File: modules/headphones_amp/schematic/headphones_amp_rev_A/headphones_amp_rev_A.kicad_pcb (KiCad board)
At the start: 2 copper layers, 150 x 100 mm, 113 parts, among them J1 AudioJack3_SwitchTR, J2 AudioJack3_SwitchTR, J3 Conn_01x02, J4 Conn_01x02, J5 Conn_01x02, J6 Conn_01x02, J7 Conn_01x02, Q1 BC140, Q10 BC548, Q11 BC548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

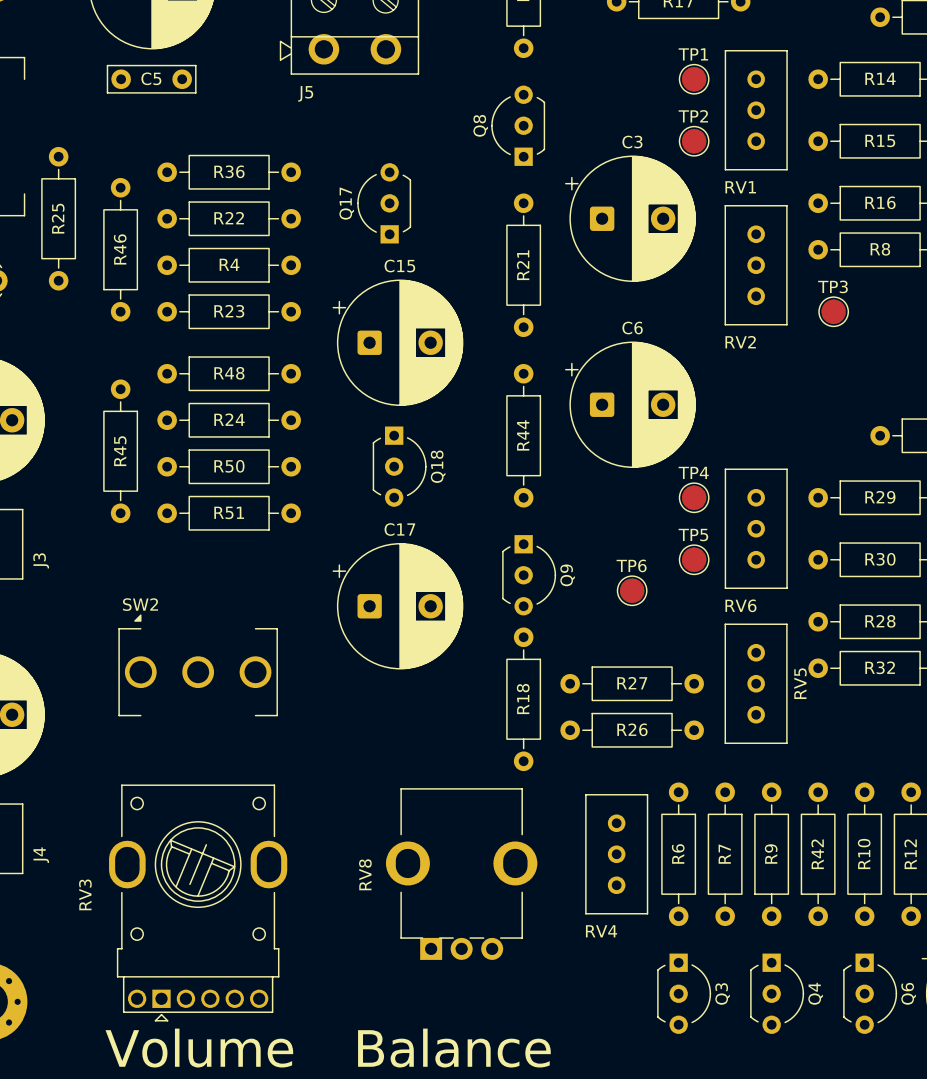
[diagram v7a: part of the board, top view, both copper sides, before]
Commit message: added a PDF export of the schematic
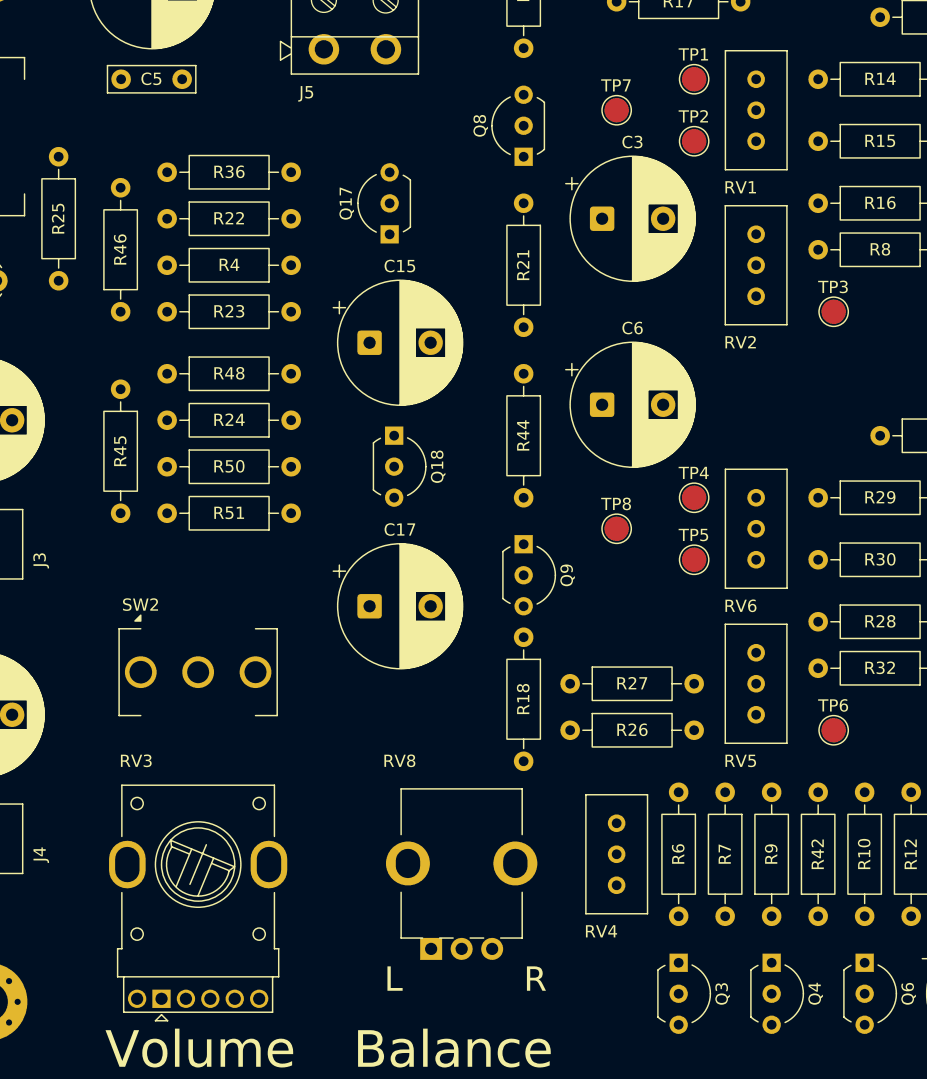
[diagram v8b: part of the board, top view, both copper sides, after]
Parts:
- added TP7: TestPoint, TestPoint:TestPoint_Pad_D2.0mm, F.Cu at (94.0, 44.5)
- added TP8: TestPoint, TestPoint:TestPoint_Pad_D2.0mm, F.Cu at (94.0, 78.7)
- moved TP6 20.1 mm to (111.8, 95.2)
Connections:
- C10 pad 2: Net-(RV3B-W) -> Net-(C10-Pad2)
- C6 pad 1: Net-(C6-Pad1) -> Net-(RV8-B)
- SW2 pad 1: Net-(Q8-C) -> Net-(RV3A-W)
- SW2 pad 2: Net-(C6-Pad1) -> Net-(C10-Pad2)
- SW2 pad 3: Net-(RV8-B) -> Net-(RV3B-W)
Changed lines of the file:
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@@
 	(net 74 "Net-(Q17-C)")
 	(net 75 "Net-(Q18-C)")
-	(net 76 "Net-(C6-Pad1)")
+	(net 76 "Net-(C10-Pad2)")
 	(footprint "Resistor_THT:R_Axial_DIN0207_L6.3mm_D2.5mm_P10.16mm_Horizontal"
 		(layer "F.Cu")
@@
 			(layers "*.Cu" "*.Mask")
 			(remove_unused_layers no)
-			(net 20 "Net-(Q8-C)")
+			(net 65 "Net-(RV3A-W)")
 			(pinfunction "1")
 			(pintype "passive")
@@
 			(layers "*.Cu" "*.Mask")
 			(remove_unused_layers no)
-			(net 76 "Net-(C6-Pad1)")
+			(net 76 "Net-(C10-Pad2)")
 			(pinfunction "2")
 			(pintype "passive")
@@
 			(layers "*.Cu" "*.Mask")
 			(remove_unused_layers no)
-			(net 31 "Net-(RV8-B)")
+			(net 66 "Net-(RV3B-W)")
 			(pinfunction "3")
 			(pintype "passive")
@@
 			(layers "*.Cu" "*.Mask")
 			(remove_unused_layers no)
-			(net 66 "Net-(RV3B-W)")
+			(net 76 "Net-(C10-Pad2)")
 			(pintype "passive")
 		)
@@
 		)
 	)
+	(footprint "TestPoint:TestPoint_Pad_D2.0mm"
+		(layer "F.Cu")
+		(at 93.98 78.74)
+		(descr "SMD pad as test Point, diameter 2.0mm")
+		(tags "test point SMD pad")
+		(property "Reference" "TP8"
+			(at 0 -1.998 0)
+			(layer "F.SilkS")
+			(effects
+				(font
+					(size 1 1)
+					(thickness 0.15)
+				)
+			)
+		)
+		(property "Value" "TestPoint"
+			(at 0 2.05 0)
+			(layer "F.Fab")
+			(hide yes)
+			(effects
+				(font
+					(size 1 1)
+					(thickness 0.15)
+				)
+			)
+		)
+		(property "Datasheet" "~"
+			(at 0 0 0)
+			(unlocked yes)
+			(layer "F.Fab")
+			(hide yes)
+			(effects
+				(font
+					(size 1.27 1.27)
+					(thickness 0.15)
+				)
+			)
+		)
+		(property "Description" "test point"
+			(at 0 0 0)
+			(unlocked yes)
+			(layer "F.Fab")
+			(hide yes)
+			(effects
+				(font
+					(size 1.27 1.27)
+					(thickness 0.15)
+				)
+			)
+		)
+		(property ki_fp_filters "Pin* Test*")
+		(sheetname "/")
+		(sheetfile "headphones_amp_rev_A.kicad_sch")
+		(attr exclude_from_pos_files)
+		(fp_circle
+			(center 0 0)
+			(end 0 1.2)
+			(stroke
+				(width 0.12)
+				(type solid)
+			)
+			(fill no)
+			(layer "F.SilkS")
+		)
+		(fp_circle
+			(center 0 0)
+			(end 1.5 0)
+			(stroke
+				(width 0.05)
+				(type solid)
+			)
+			(fill no)
+			(layer "F.CrtYd")
+		)
+		(fp_text user "${REFERENCE}"
+			(at 0 -2 0)
+			(layer "F.Fab")
+			(effects
+				(font
+					(size 1 1)
+					(thickness 0.15)
+				)
+			)
+		)
+		(pad "1" smd circle
+			(at 0 0)
+			(size 2 2)
+			(layers "F.Cu" "F.Mask")
+			(net 75 "Net-(Q18-C)")
+			(pinfunction "1")
+			(pintype "passive")
+		)
+		(embedded_fonts no)
+	)
 	(footprint "LED_THT:LED_D3.0mm"
 		(layer "F.Cu")
@@
 			(at 2.5 6.25 0)
 			(layer "F.Fab")
+			(hide yes)
 			(effects
 				(font
@@
 			(remove_unused_layers no)
 			(roundrect_rratio 0.125)
-			(net 76 "Net-(C6-Pad1)")
+			(net 31 "Net-(RV8-B)")
 			(pintype "passive")
 		)
@@
 		(tags "Potentiometer vertical Bourns PTV09A-1 Single")
 		(property "Reference" "RV8"
-			(at 6.05 -5.35 90)
+			(at 15.374 -2.58 180)
 			(layer "F.SilkS")
 			(effects
@@
 			(at 6.05 10.35 90)
 			(layer "F.Fab")
+			(hide yes)
 			(effects
 				(font
@@
 			(at 2.5 6.25 0)
 			(layer "F.Fab")
+			(hide yes)
 			(effects
 				(font
@@
 	(footprint "TestPoint:TestPoint_Pad_D2.0mm"
 		(layer "F.Cu")
-		(at 95.25 83.82)
+		(at 111.76 95.25)
 		(descr "SMD pad as test Point, diameter 2.0mm")
 		(tags "test point SMD pad")
@@
 			(at 0 2.05 0)
 			(layer "F.Fab")
+			(hide yes)
 			(effects
 				(font
@@
 		(tags "PTV112-4 Dual gang")
 		(property "Reference" "RV3"
-			(at 8.5 -6.2 90)
+			(at 19.4625 -2.08 180)
 			(layer "F.SilkS")
 			(effects
@@
 			(at -2.54 3.67 90)
 			(layer "F.Fab")
+			(hide yes)
 			(effects
 				(font
@@
 		(tags "Potentiometer vertical Bourns 3296W")
 		(property "Reference" "RV5"
-			(at -2.54 -3.66 90)
+			(at 3.81 1.27 180)
 			(layer "F.SilkS")
 			(effects
@@
 		)
 	)
+	(footprint "TestPoint:TestPoint_Pad_D2.0mm"
+		(layer "F.Cu")
+		(at 93.98 44.45)
+		(descr "SMD pad as test Point, diameter 2.0mm")
+		(tags "test point SMD pad")
+		(property "Reference" "TP7"
+			(at 0 -1.998 0)
+			(layer "F.SilkS")
+			(effects
+				(font
+					(size 1 1)
+					(thickness 0.15)
+				)
+			)
+		)
+		(property "Value" "TestPoint"
+			(at 0 2.05 0)
+			(layer "F.Fab")
+			(hide yes)
+			(effects
+				(font
+					(size 1 1)
+					(thickness 0.15)
+				)
+			)
+		)
+		(property "Datasheet" "~"
+			(at 0 0 0)
+			(unlocked yes)
+			(layer "F.Fab")
+			(hide yes)
+			(effects
+				(font
+					(size 1.27 1.27)
+					(thickness 0.15)
+				)
+			)
+		)
+		(property "Description" "test point"
+			(at 0 0 0)
+			(unlocked yes)
+			(layer "F.Fab")
+			(hide yes)
+			(effects
+				(font
+					(size 1.27 1.27)
+					(thickness 0.15)
+				)
+			)
+		)
+		(property ki_fp_filters "Pin* Test*")
+		(sheetname "/")
+		(sheetfile "headphones_amp_rev_A.kicad_sch")
+		(attr exclude_from_pos_files)
+		(fp_circle
+			(center 0 0)
+			(end 0 1.2)
+			(stroke
+				(width 0.12)
+				(type solid)
+			)
+			(fill no)
+			(layer "F.SilkS")
+		)
+		(fp_circle
+			(center 0 0)
+			(end 1.5 0)
+			(stroke
+				(width 0.05)
+				(type solid)
+			)
+			(fill no)
+			(layer "F.CrtYd")
+		)
+		(fp_text user "${REFERENCE}"
+			(at 0 -2 0)
+			(layer "F.Fab")
+			(effects
+				(font
+					(size 1 1)
+					(thickness 0.15)
+				)
+			)
+		)
+		(pad "1" smd circle
+			(at 0 0)
+			(size 2 2)
+			(layers "F.Cu" "F.Mask")
+			(net 74 "Net-(Q17-C)")
+			(pinfunction "1")
+			(pintype "passive")
+		)
+		(embedded_fonts no)
+	)
 	(footprint "ProjectLib_Transient:WuerthElectronik_WR_TBL_Series_2109_1x02_P2.54mm_Horizontal"
 		(layer "F.Cu")
@@
 		(layer "Edge.Cuts")
 	)
+	(gr_text "L\n"
+		(at 74.93 116.84 0)
+		(layer "F.SilkS")
+		(effects
+			(font
+				(size 2 2)
+				(thickness 0.25)
+			)
+			(justify left bottom)
+		)
+	)
 	(gr_text "Volume"
 		(at 52.07 123.19 0)
@@
 			)
 			(justify left bottom)
+		)
+	)
+	(gr_text "R"
+		(at 86.36 116.84 0)
+		(layer "F.SilkS")
+		(effects
+			(font
+				(size 2 2)
+				(thickness 0.25)
+			)
+			(justify left bottom)
